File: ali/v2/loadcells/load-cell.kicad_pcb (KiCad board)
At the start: 4 copper layers, 76 x 76 mm, 130 parts, among them J1 Conn_02x01, J10 Conn_01x04_MountingPin, J11 Conn_01x04_MountingPin, J12 Conn_01x04_MountingPin, J13 Conn_01x04_MountingPin, J14 Conn_01x04_MountingPin, J2 Conn_01x05_MountingPin, J3 USB_C_Receptacle_USB2.0_16P, J4 Conn_01x15, J5 Conn_02x09_Counter_Clockwise, J6 Screw_Terminal_01x02, J7 Conn_01x03, J8 Hanrun HY951180A, J9 Conn_01x04_MountingPin, SW1 SKRPANE010, U1 STM32H563RIVx, U2 AP2112K-3.3, U3 TJA1462ATK, U4 LAN8742AI, U5 ADS124S08, Y1 25 MHz, Y2 25 MHz

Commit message: mfw tcs
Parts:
- C27, C28, C8, C9: value 10pF -> 15pF
- D10, D12, D14, D16, D6, D8: value SMF5V0A -> SMF7V0A
- J10, J11, J12, J13, J14, J9: value Conn_01x04_MountingPin -> Conn_01x04
- J2: value Conn_01x05_MountingPin -> Conn_01x05
- J8: value Hanrun HY951180A -> Vertical Ethernet
- U1: value STM32H563RIVx -> STM32H563RIV6
- U3: footprint Package_SON:HVSON-8-1EP_3x3mm_P0.65mm_EP1.6x2.4mm -> APRL_Package_QFN:HVSON-8-1EP_3x3mm_P0.65mm_EP1.6x2.4mm_ThermalVias
- U4: footprint Package_DFN_QFN:VQFN-24-1EP_4x4mm_P0.5mm_EP2.5x2.5mm_ThermalVias -> APRL_Package_QFN:VQFN-24-1EP_4x4mm_P0.5mm_EP2.5x2.5mm_ThermalVias
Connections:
- U5 pad 17: unconnected-(U5-CLK-Pad17) -> GND

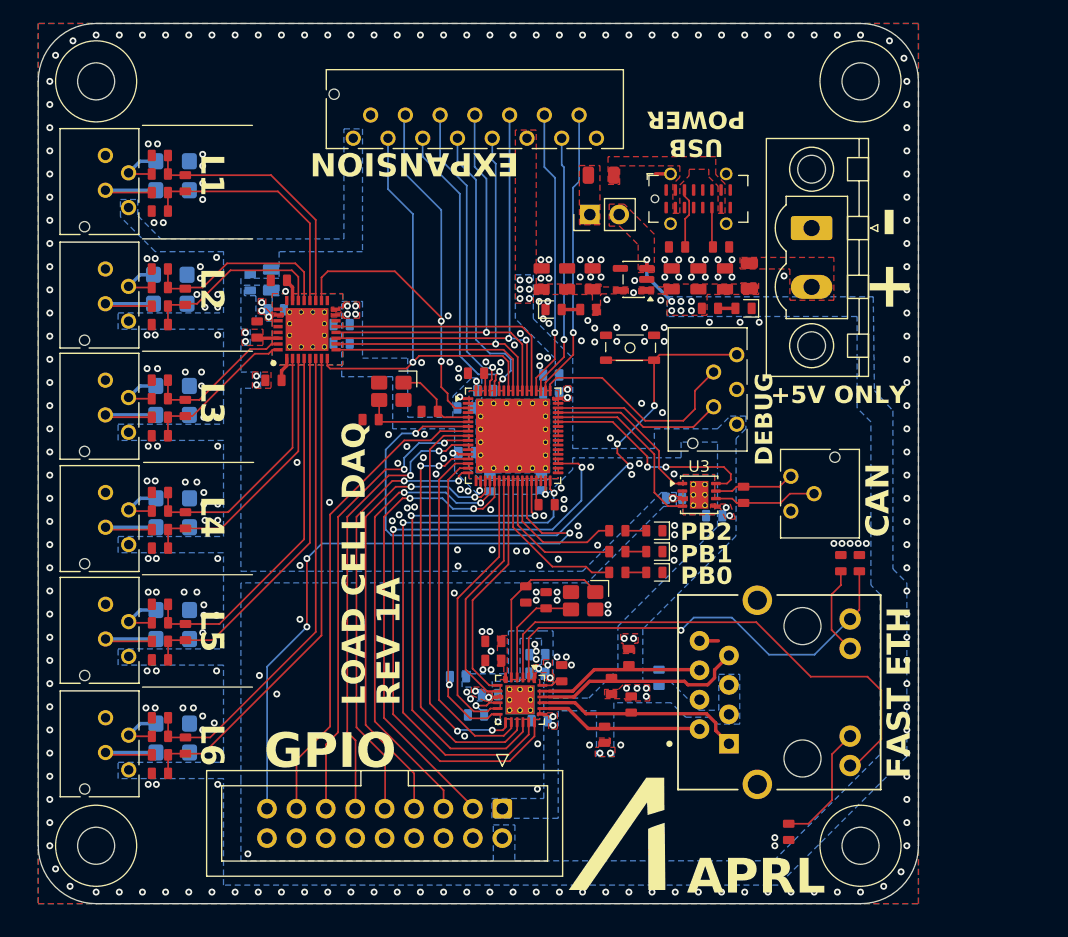
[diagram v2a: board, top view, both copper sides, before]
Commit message: Update load cells to use timer pins
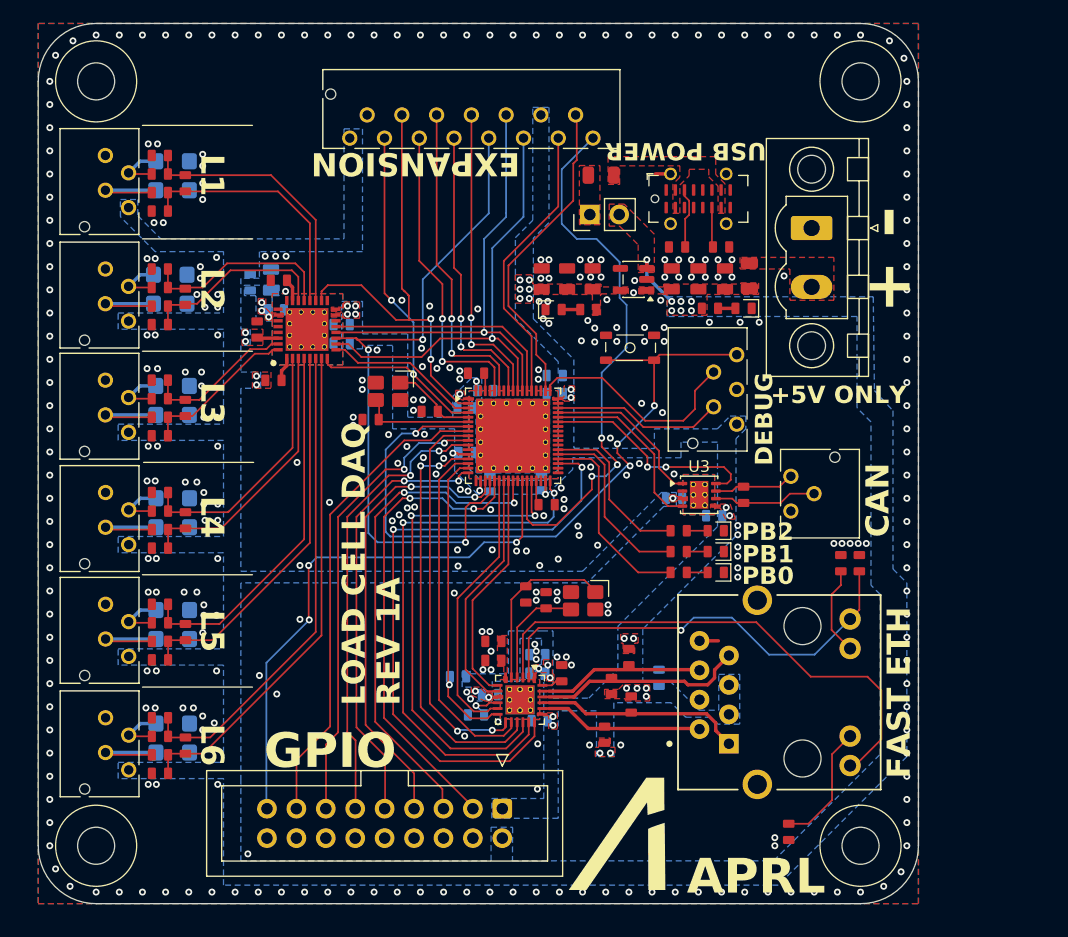
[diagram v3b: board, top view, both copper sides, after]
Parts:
- moved D3 5.30 mm to (154.2, 110.7)
- moved D4 5.30 mm to (154.2, 108.9)
- moved D5 5.30 mm to (154.2, 107.1)
- moved R5 5.30 mm to (151.0, 110.7)
- moved R6 5.30 mm to (151.0, 108.9)
- moved R7 5.30 mm to (151.0, 107.1)
- moved C6 0.30 mm to (140.3, 95.3)
- moved C1 0.30 mm to (140.3, 93.7)
- moved J4 0.30 mm to (122.6, 73.2)
- moved Y1 0.29 mm to (125.9, 95.0)
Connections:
- net /Microcontroller/PA15 renamed /Microcontroller/TIM2_CH1
- net /Microcontroller/PA3 renamed /Microcontroller/TIM2_CH4
- net /Microcontroller/PB9 renamed /Microcontroller/UART4_TX
- J4 pad 10: /ADC/SCLK -> /ADC/MISO
- J4 pad 11: +3.3V -> /ADC/MOSI
- J4 pad 12: /Microcontroller/PC11 -> +3.3V
- J4 pad 13: /Microcontroller/PC10 -> /Microcontroller/PC12
- J4 pad 15: GND -> /Microcontroller/TIM2_CH3
- J4 pad 6: /Microcontroller/PE0 -> /Microcontroller/UART4_RX
- J4 pad 7: /Microcontroller/PB8 -> /Microcontroller/I2C1_SCA
- J4 pad 8: /ADC/MISO -> /Microcontroller/I2C1_SCL
- J4 pad 9: /ADC/MOSI -> /ADC/SCLK
- J5 pad 17: /Microcontroller/PB10 -> /Microcontroller/PB2
- J5 pad 5: /Microcontroller/PA5 -> /Microcontroller/PB0
- U1 pad 2: unconnected-(U1-PC13-Pad2) -> /ADC/RESET
- U1 pad 21: /Microcontroller/PA5 -> /ADC/SCLK
- U1 pad 26: /Microcontroller/USER_LED_1 -> /Microcontroller/PB0
- U1 pad 27: /Microcontroller/USER_LED_2 -> unconnected-(U1-PB1-Pad27)
- U1 pad 28: /Microcontroller/USER_LED_3 -> /Microcontroller/PB2
- U1 pad 29: /Microcontroller/PB10 -> /Microcontroller/TIM2_CH3
- U1 pad 3: /ADC/RESET -> /ADC/CS
- U1 pad 38: unconnected-(U1-PD11-Pad38) -> /Microcontroller/USER_LED_1
- U1 pad 39: unconnected-(U1-PD12-Pad39) -> /Microcontroller/USER_LED_2
- U1 pad 4: unconnected-(U1-PC15-Pad4) -> /ADC/START
- U1 pad 40: unconnected-(U1-PC6-Pad40) -> /Microcontroller/USER_LED_3
- U1 pad 56: /ADC/DRDY -> /Microcontroller/PC12
- U1 pad 57: /ADC/SCLK -> /ADC/DRDY
- U1 pad 60: /ADC/CS -> /Microcontroller/I2C1_SCL
- U1 pad 61: /ADC/START -> /Microcontroller/I2C1_SCA
- U1 pad 63: /Microcontroller/PB8 -> /Microcontroller/UART4_RX
- U1 pad 65: /Microcontroller/PE0 -> unconnected-(U1-PE0-Pad65)
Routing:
- net /Microcontroller/PB10: track 54.6 -> 0.00 mm, vias 3 -> 0
- net /Microcontroller/TIM2_CH3: track 0.00 -> 48.5 mm, vias 0 -> 3
- net /Microcontroller/PB2: track 0.00 -> 46.9 mm, vias 0 -> 3
- net /Microcontroller/PB0: track 0.00 -> 42.8 mm, vias 0 -> 2
- net /Microcontroller/PA5: track 40.8 -> 0.00 mm, vias 2 -> 0
- net /Microcontroller/UART4_RX: track 0.00 -> 27.9 mm, vias 0 -> 2
- net /Microcontroller/I2C1_SCL: track 0.00 -> 26.4 mm, vias 0 -> 2
- net /Microcontroller/PE0: track 26.3 -> 0.00 mm, vias 1 -> 0
- net /Microcontroller/I2C1_SCA: track 0.00 -> 25.1 mm, vias 0 -> 2
- net /Microcontroller/PB8: track 24.9 -> 0.00 mm, vias 1 -> 0
- net /Microcontroller/PC11: track 24.9 -> 0.00 mm, vias 1 -> 0
- net /Microcontroller/PC12: track 0.00 -> 24.8 mm
- net /Microcontroller/PC10: track 22.7 -> 0.00 mm, vias 1 -> 0
- net /ADC/SCLK: track 40.2 -> 60.1 mm, vias 2 -> 3
- net /ADC/CS: track 18.3 -> 13.5 mm
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
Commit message: Swap to sync'd ADS1261s on LC, update README and clean up Just scripts, some frame changes too.
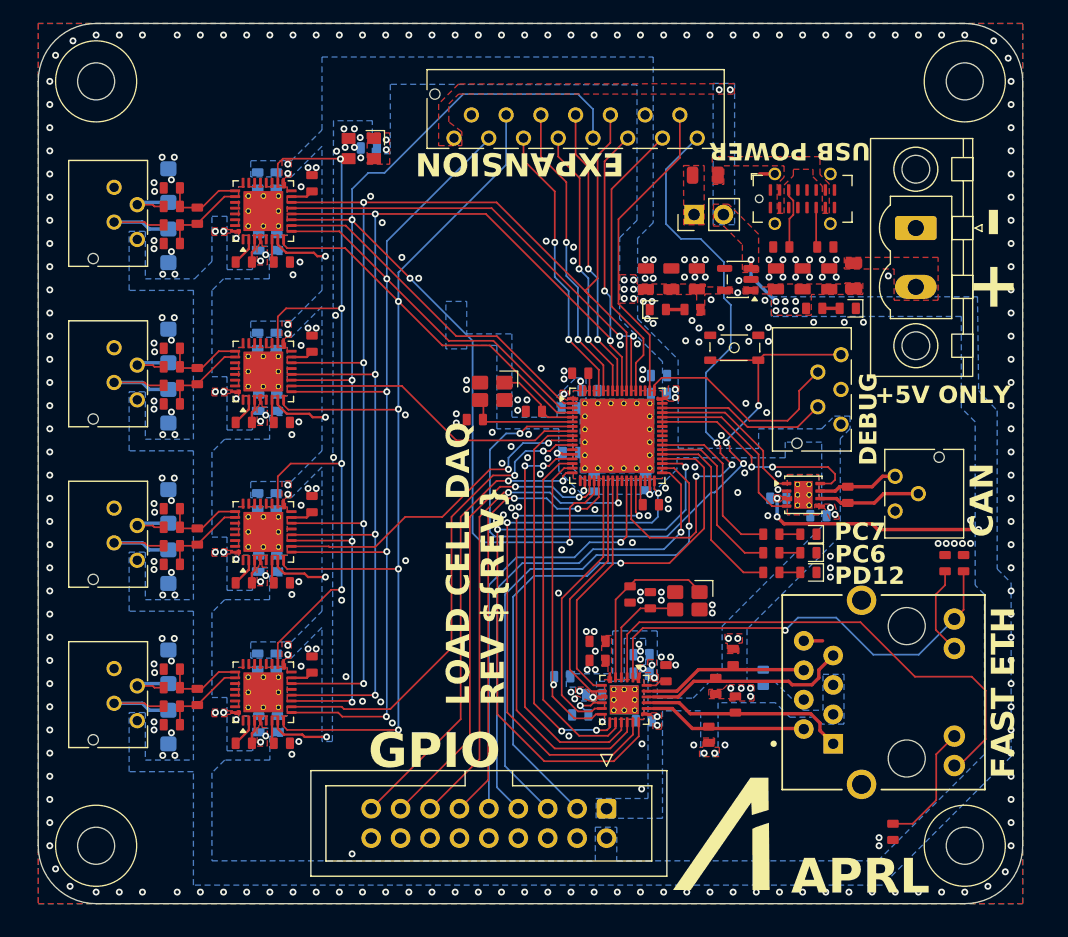
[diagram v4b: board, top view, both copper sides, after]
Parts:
- removed the C29 at (106.2, 128.1)
- removed D14, D15, D16, D17: SMF7V0A, Diode_SMD:D_SMF
- removed J13, J14: Conn_01x04, APRL_Connector_Molex:Molex_CLIK-Mate_503159-0401_1x04-1MP_P1.50mm_Vertical
- removed R27, R28, R29, R30, R31, R32: 1k, APRL_Passive:R_0603
- added C12: 100nF, APRL_Passive:C_0603, B.Cu at (124.3, 74.1)
- added C53: 1uF, APRL_Passive:C_0603, B.Cu at (114.7, 104.6)
- added C54: 1nF, APRL_Passive:C_0603, F.Cu at (107.2, 110.0)
- added C55: 10nF, APRL_Passive:C_0603, F.Cu at (109.4, 107.6)
- added C56: 1nF, APRL_Passive:C_0603, F.Cu at (107.2, 105.2)
- added C57: 4.7nF, APRL_Passive:C_0603, F.Cu at (113.5, 111.6)
- added C58: 1uF, APRL_Passive:C_0603, F.Cu at (119.3, 104.8)
- added C59: 10uF, APRL_Passive:C_0603, F.Cu at (116.7, 111.6)
- added C60: 1uF, APRL_Passive:C_0603, B.Cu at (116.4, 123.8)
- added C61: 100nF, APRL_Passive:C_0603, B.Cu at (114.7, 123.8)
- added C62: 100nF, APRL_Passive:C_0603, B.Cu at (116.3, 118.4)
- added C63: 1uF, APRL_Passive:C_0603, B.Cu at (114.7, 118.4)
- added C64: 1nF, APRL_Passive:C_0603, F.Cu at (107.2, 123.9)
- added C65: 10nF, APRL_Passive:C_0603, F.Cu at (109.4, 121.5)
- added C66: 1nF, APRL_Passive:C_0603, F.Cu at (107.2, 119.1)
- added C67: 4.7nF, APRL_Passive:C_0603, F.Cu at (113.5, 125.5)
- added C68: 1uF, APRL_Passive:C_0603, F.Cu at (119.3, 118.7)
- added C69: 10uF, APRL_Passive:C_0603, F.Cu at (116.7, 125.5)
- added U6: ADS1261, APRL_Package_QFN:Texas_RHB0032E_VQFN-32-1EP_5x5mm_P0.5mm_EP3.45x3.45mm_ThermalVias, F.Cu at (115.1, 93.4)
- added U7: ADS1261, APRL_Package_QFN:Texas_RHB0032E_VQFN-32-1EP_5x5mm_P0.5mm_EP3.45x3.45mm_ThermalVias, F.Cu at (115.1, 107.2)
- added U8: ADS1261, APRL_Package_QFN:Texas_RHB0032E_VQFN-32-1EP_5x5mm_P0.5mm_EP3.45x3.45mm_ThermalVias, F.Cu at (115.1, 121.1)
- added Y2: 7.3278 MHz, APRL_Passive:Oscillator_SCTF_SX3M_3.2x2.5mm, F.Cu at (123.6, 74.1)
- C30, C40, C43: value 1nF -> 1uF; moved to B.Cu
- C31, C32, C41, C42: value 10nF -> 100nF; moved to B.Cu
- C34: value 100nF -> 1nF; moved to F.Cu
- C35: value 100nF -> 10nF; moved to F.Cu
- C36: value 22uF -> 1nF; footprint APRL_Passive:C_0805 -> APRL_Passive:C_0603; moved to F.Cu
- C37, C47: value 1nF -> 4.7nF
- C38: value 1nF -> 1uF
- C39: value 1nF -> 10uF
- C45: value 1uF -> 10nF
- C48: value 100nF -> 1uF
- C49: value 10nF -> 10uF
- C50: value 10nF -> 1uF; moved to B.Cu
- C51, C52: value 1nF -> 100nF; moved to B.Cu
- R21: value 10R -> 1k; moved to F.Cu
- R24: value 100k -> 1k
- U5: value ADS124S08 -> ADS1261; footprint APRL_Package:QFN-32_EP_5.8x5.8_Pitch0.5mm -> APRL_Package_QFN:Texas_RHB0032E_VQFN-32-1EP_5x5mm_P0.5mm_EP3.45x3.45mm_ThermalVias
- moved D7 46.5 mm to (106.9, 77.3), turned to 90 degrees
- moved J9 45.8 mm to (104.3, 82.0)
- moved R19 45.8 mm to (107.2, 80.7)
- moved C31 43.9 mm to (114.7, 82.2), turned to 90 degrees
- moved D6 43.8 mm to (106.9, 82.5), turned to -90 degrees
- moved C37 40.0 mm to (113.5, 83.9)
- moved D12 36.6 mm to (106.9, 124.1), turned to -90 degrees
- moved C39 35.9 mm to (116.7, 83.9), turned to 0 degrees
- moved J12 34.5 mm to (104.3, 123.5)
- moved D13 33.9 mm to (106.9, 118.9), turned to 90 degrees
- moved C50 33.8 mm to (116.3, 110.0), turned to 90 degrees
- moved R26 33.0 mm to (107.2, 120.7)
- moved R22 31.9 mm to (107.2, 93.0)
- moved C52 31.5 mm to (116.3, 104.6), turned to -90 degrees
- moved C43 24.3 mm to (114.7, 90.7), turned to -90 degrees
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- renumbered C12 to C13, C13 to C14, C14 to C15, C15 to C16, C16 to C17, C17 to C18, C18 to C19, C19 to C20, C20 to C21, C21 to C22, C22 to C23, C23 to C24, C24 to C25, C25 to C26, C26 to C27, C27 to C28, C28 to C29, D3 to D1, D4 to D2, D1 to D3, D2 to D4, R5 to R3, R3 to R4, R4 to R5, Y2 to Y3
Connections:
- C30 pad 1: /ADC/AIN6 -> +5V
- C31 pad 1: /ADC/AIN1 -> +5V
- C31 pad 2: /ADC/AIN0 -> GND
- C32 pad 1: /ADC/AIN7 -> +3.3V
- C32 pad 2: /ADC/AIN6 -> GND
- C34 pad 1: +3.3V -> Net-(U5-AIN6)
- C35 pad 1: Net-(U5-AVDD) -> Net-(U5-AIN7)
- C35 pad 2: GND -> Net-(U5-AIN6)
- C36 pad 1: Net-(U5-AVDD) -> GND
- C36 pad 2: GND -> Net-(U5-AIN7)
- C37 pad 1: GND -> Net-(U5-CAPP)
- C37 pad 2: /ADC/AIN1 -> Net-(U5-CAPN)
- C38 pad 1: GND -> Net-(U5-BYPASS)
- C38 pad 2: /ADC/AIN7 -> GND
- C39 pad 1: /ADC/AIN2 -> Net-(U5-REFOUT)
- C40 pad 1: /ADC/AIN8 -> +5V
- C41 pad 1: /ADC/AIN3 -> +5V
- C41 pad 2: /ADC/AIN2 -> GND
- C42 pad 1: /ADC/AIN9 -> +3.3V
- C42 pad 2: /ADC/AIN8 -> GND
- C43 pad 1: GND -> +3.3V
- C43 pad 2: /ADC/AIN3 -> GND
- C44 pad 1: GND -> Net-(U6-AIN6)
- C44 pad 2: /ADC/AIN9 -> GND
- C45 pad 1: Net-(U5-REFOUT) -> Net-(U6-AIN7)
- C45 pad 2: GND -> Net-(U6-AIN6)
- C46 pad 1: /ADC/AIN4 -> GND
- C46 pad 2: GND -> Net-(U6-AIN7)
- C47 pad 1: /ADC/AIN10 -> Net-(U6-CAPP)
- C47 pad 2: GND -> Net-(U6-CAPN)
- C48 pad 1: +5V -> Net-(U6-BYPASS)
- C49 pad 1: /ADC/AIN5 -> Net-(U6-REFOUT)
- C49 pad 2: /ADC/AIN4 -> GND
- C50 pad 1: /ADC/AIN11 -> +5V
- C50 pad 2: /ADC/AIN10 -> GND
- C51 pad 1: GND -> +5V
- C51 pad 2: /ADC/AIN5 -> GND
- C52 pad 1: GND -> +3.3V
- C52 pad 2: /ADC/AIN11 -> GND
- J5 pad 11: /Microcontroller/PC3 -> /Microcontroller/PA6
- J5 pad 13: /Microcontroller/PC2 -> /Microcontroller/PB0
- J5 pad 15: /Microcontroller/PC0 -> /Microcontroller/PA4
- J5 pad 17: /Microcontroller/PB2 -> /Microcontroller/TIM2_CH4
- J5 pad 3: /Microcontroller/PA6 -> /Microcontroller/PD11
- J5 pad 5: /Microcontroller/PB0 -> /Microcontroller/PB14
- J5 pad 7: /Microcontroller/PA4 -> /Microcontroller/PB13
- J5 pad 9: /Microcontroller/TIM2_CH4 -> /Microcontroller/PB2
- R19 pad 2: /ADC/AIN0 -> Net-(U5-AIN6)
- R20 pad 1: Net-(D8-A1) -> Net-(D7-A1)
- R20 pad 2: /ADC/AIN6 -> Net-(U5-AIN7)
- R21 pad 1: Net-(U5-AVDD) -> Net-(D8-A1)
- R21 pad 2: +5V -> Net-(U6-AIN6)
- R22 pad 1: Net-(D7-A1) -> Net-(D9-A1)
- R22 pad 2: /ADC/AIN1 -> Net-(U6-AIN7)
- R23 pad 1: Net-(D9-A1) -> Net-(D10-A1)
- R23 pad 2: /ADC/AIN7 -> Net-(U7-AIN6)
- R24 pad 1: +5V -> Net-(D11-A1)
- R24 pad 2: Net-(U5-AINCOM) -> Net-(U7-AIN7)
- R25 pad 1: Net-(D10-A1) -> Net-(D12-A1)
- R25 pad 2: /ADC/AIN2 -> Net-(U8-AIN6)
- R26 pad 1: Net-(D12-A1) -> Net-(D13-A1)
- R26 pad 2: /ADC/AIN8 -> Net-(U8-AIN7)
- U1 pad 10: /Microcontroller/PC2 -> /ADC2/CS
- U1 pad 11: /Microcontroller/PC3 -> /ADC3/CS
- U1 pad 2: /ADC/RESET -> /ADC/CS
- U1 pad 3: /ADC/CS -> /ADC/START
- U1 pad 35: unconnected-(U1-PB13-Pad35) -> /Microcontroller/PB13
- U1 pad 36: unconnected-(U1-PB14-Pad36) -> /Microcontroller/PB14
- U1 pad 38: /Microcontroller/USER_LED_1 -> /Microcontroller/PD11
- U1 pad 39: /Microcontroller/USER_LED_2 -> /Microcontroller/USER_LED_1
- U1 pad 4: /ADC/START -> /ADC/RESET
- U1 pad 40: /Microcontroller/USER_LED_3 -> /Microcontroller/USER_LED_2
- U1 pad 41: unconnected-(U1-PC7-Pad41) -> /Microcontroller/USER_LED_3
- U1 pad 54: /Microcontroller/PC10 -> unconnected-(U1-PC10-Pad54)
- U1 pad 55: /Microcontroller/PC11 -> unconnected-(U1-PC11-Pad55)
- U1 pad 8: /Microcontroller/PC0 -> /ADC1/CS
- U5 pad 1: Net-(U5-AINCOM) -> GND
- U5 pad 10: /ADC/MOSI -> /ADC/CS
- U5 pad 12: /ADC/MISO -> /ADC/MOSI
- U5 pad 14: GND -> /ADC/MISO
- U5 pad 15: +3.3V -> Net-(U5-BYPASS)
- U5 pad 16: +3.3V -> GND
- U5 pad 17: GND -> +3.3V
- U5 pad 18: /ADC/RESET -> /ADC/CLK
- U5 pad 19: /ADC/AIN11 -> unconnected-(U5-NC-Pad19)
- U5 pad 2: /ADC/AIN5 -> Net-(U5-CAPP)
- U5 pad 20: /ADC/AIN10 -> unconnected-(U5-NC-Pad20)
- U5 pad 21: /ADC/AIN9 -> unconnected-(U5-NC-Pad21)
- U5 pad 22: /ADC/AIN8 -> unconnected-(U5-NC-Pad22)
- U5 pad 23: Net-(U5-REFOUT) -> GND
- U5 pad 25: unconnected-(U5-NC-Pad25) -> Net-(U5-AIN7)
- U5 pad 26: Net-(U5-AVDD) -> Net-(U5-AIN6)
- U5 pad 3: /ADC/AIN4 -> Net-(U5-CAPN)
- U5 pad 30: +5V -> GND
- U5 pad 31: /ADC/AIN7 -> GND
- U5 pad 32: /ADC/AIN6 -> +5V
- U5 pad 4: /ADC/AIN3 -> +5V
- U5 pad 5: /ADC/AIN2 -> GND
- U5 pad 6: /ADC/AIN1 -> Net-(U5-REFOUT)
- U5 pad 7: /ADC/AIN0 -> +3.3V
- U5 pad 8: /ADC/START -> /ADC/RESET
- U5 pad 9: /ADC/CS -> /ADC/START
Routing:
- net /ADC/RESET: track 38.8 -> 119.9 mm, vias 2 -> 4
- net /ADC/MOSI: track 38.8 -> 118.7 mm, vias 1 -> 6
- net /ADC/SCLK: track 60.1 -> 139.3 mm, vias 3 -> 6
- net /ADC/MISO: track 39.6 -> 115.7 mm, vias 1 -> 4
- net /ADC/START: track 35.8 -> 109.0 mm, vias 2 -> 4
- net /ADC/CLK: track 0.00 -> 70.2 mm, vias 0 -> 4
- net /Microcontroller/PD11: track 0.00 -> 48.7 mm, vias 0 -> 1
- net /Microcontroller/PB14: track 0.00 -> 45.9 mm, vias 0 -> 1
- net /Microcontroller/PB13: track 0.00 -> 43.8 mm, vias 0 -> 1
- net /ADC/AIN0: track 42.9 -> 0.00 mm
- net /Microcontroller/PC0: track 42.0 -> 0.00 mm
- net /ADC/AIN1: track 41.6 -> 0.00 mm
- net /ADC3/CS: track 0.00 -> 41.1 mm, vias 0 -> 2
- net /Microcontroller/PC2: track 40.7 -> 0.00 mm, vias 2 -> 0
- net /Microcontroller/PC3: track 39.7 -> 0.00 mm, vias 2 -> 0
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- removed copper zone on B.Cu, net Net-(U5-AVDD)
- removed copper zone on F.Cu, net Net-(U5-AVDD)
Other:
- board size 76 x 76 mm -> 85 x 76 mm
- board text added: "PC6"
- board text added: "PC7"
- board text added: "PD12"
- board text added: "REV ${REV}"
- board text removed: "L1"
- board text removed: "L2"
- board text removed: "L3"
- board text removed: "L4"
- board text removed: "L5"
- board text removed: "L6"
- board text removed: "PB0"
- board text removed: "PB1"
- board text removed: "PB2"
- board text removed: "REV 1A"

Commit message: Minor thermocouple updates
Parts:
- added R28: 22R, APRL_Passive:R_0603, F.Cu at (121.7, 73.3)
- moved Y2 4.06 mm to (122.9, 70.1)
- moved C12 2.97 mm to (123.9, 71.1)
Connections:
- net /ADC/CS renamed /ADC 1/CS
- net /ADC/DRDY renamed /ADC 1/DRDY
- net /ADC/MISO renamed /ADC 1/MISO
- net /ADC/MOSI renamed /ADC 1/MOSI
- net /ADC/RESET renamed /ADC 1/RESET
- net /ADC/SCLK renamed /ADC 1/SCLK
- net /ADC/START renamed /ADC 1/START
- net /ADC1/CS renamed /ADC 2/CS
- net /ADC1/DRDY renamed /ADC 2/DRDY
- net /ADC2/CS renamed /ADC 3/CS
- net /ADC2/DRDY renamed /ADC 3/DRDY
- net /ADC3/CS renamed /ADC 4/CS
- net /ADC3/DRDY renamed /ADC 4/DRDY
- U5 pad 18: /ADC/CLK -> /ADC 1/CLK
- U5 pad 23: GND -> unconnected-(U5-AIN9-Pad23)
- U5 pad 24: GND -> unconnected-(U5-AIN8-Pad24)
- U5 pad 27: GND -> unconnected-(U5-AIN5/ACX2-Pad27)
- U5 pad 28: GND -> unconnected-(U5-AIN4/ACX1-Pad28)
- U5 pad 29: GND -> unconnected-(U5-AIN3/~{ACX2}-Pad29)
- U5 pad 30: GND -> unconnected-(U5-AIN2/~{ACX1}-Pad30)
- U6 pad 18: /ADC/CLK -> /ADC 1/CLK
- U6 pad 23: GND -> unconnected-(U6-AIN9-Pad23)
- U6 pad 24: GND -> unconnected-(U6-AIN8-Pad24)
- U6 pad 27: GND -> unconnected-(U6-AIN5/ACX2-Pad27)
- U6 pad 28: GND -> unconnected-(U6-AIN4/ACX1-Pad28)
- U6 pad 29: GND -> unconnected-(U6-AIN3/~{ACX2}-Pad29)
- U6 pad 30: GND -> unconnected-(U6-AIN2/~{ACX1}-Pad30)
- U7 pad 18: /ADC/CLK -> /ADC 1/CLK
- U7 pad 23: GND -> unconnected-(U7-AIN9-Pad23)
- U7 pad 24: GND -> unconnected-(U7-AIN8-Pad24)
- U7 pad 27: GND -> unconnected-(U7-AIN5/ACX2-Pad27)
- U7 pad 28: GND -> unconnected-(U7-AIN4/ACX1-Pad28)
- U7 pad 29: GND -> unconnected-(U7-AIN3/~{ACX2}-Pad29)
- U7 pad 30: GND -> unconnected-(U7-AIN2/~{ACX1}-Pad30)
- U8 pad 18: /ADC/CLK -> /ADC 1/CLK
- U8 pad 23: GND -> unconnected-(U8-AIN9-Pad23)
- U8 pad 24: GND -> unconnected-(U8-AIN8-Pad24)
- U8 pad 27: GND -> unconnected-(U8-AIN5/ACX2-Pad27)
- U8 pad 28: GND -> unconnected-(U8-AIN4/ACX1-Pad28)
- U8 pad 29: GND -> unconnected-(U8-AIN3/~{ACX2}-Pad29)
- U8 pad 30: GND -> unconnected-(U8-AIN2/~{ACX1}-Pad30)
- Y2 pad 3: /ADC/CLK -> Net-(Y2-OUT)
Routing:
- net /ADC 1/CLK: track 0.00 -> 71.2 mm, vias 0 -> 4
- net /ADC/CLK: track 70.2 -> 0.00 mm, vias 4 -> 0
- net /ADC 1/START: track 109.0 -> 113.8 mm
- net /ADC 1/RESET: track 119.9 -> 124.0 mm
- net /ADC 1/SCLK: track 139.3 -> 141.8 mm
- net /ADC 1/MOSI: track 118.7 -> 120.8 mm
- net Net-(Y2-OUT): track 0.00 -> 1.67 mm
- net /ADC 1/MISO: track 115.7 -> 117.3 mm
- net GND: vias 364 -> 383
- net +3.3V: vias 44 -> 45
- net (no net): vias 0 -> 1
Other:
- board text added: "L1"
- board text added: "L2"
- board text added: "L3"
- board text added: "L4"
